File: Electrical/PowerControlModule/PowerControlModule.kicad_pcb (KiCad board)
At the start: 2 copper layers, 2 parts, among them Q1 IPP120P04P4L03AKSA1, Q2 IPP120P04P4L03AKSA1

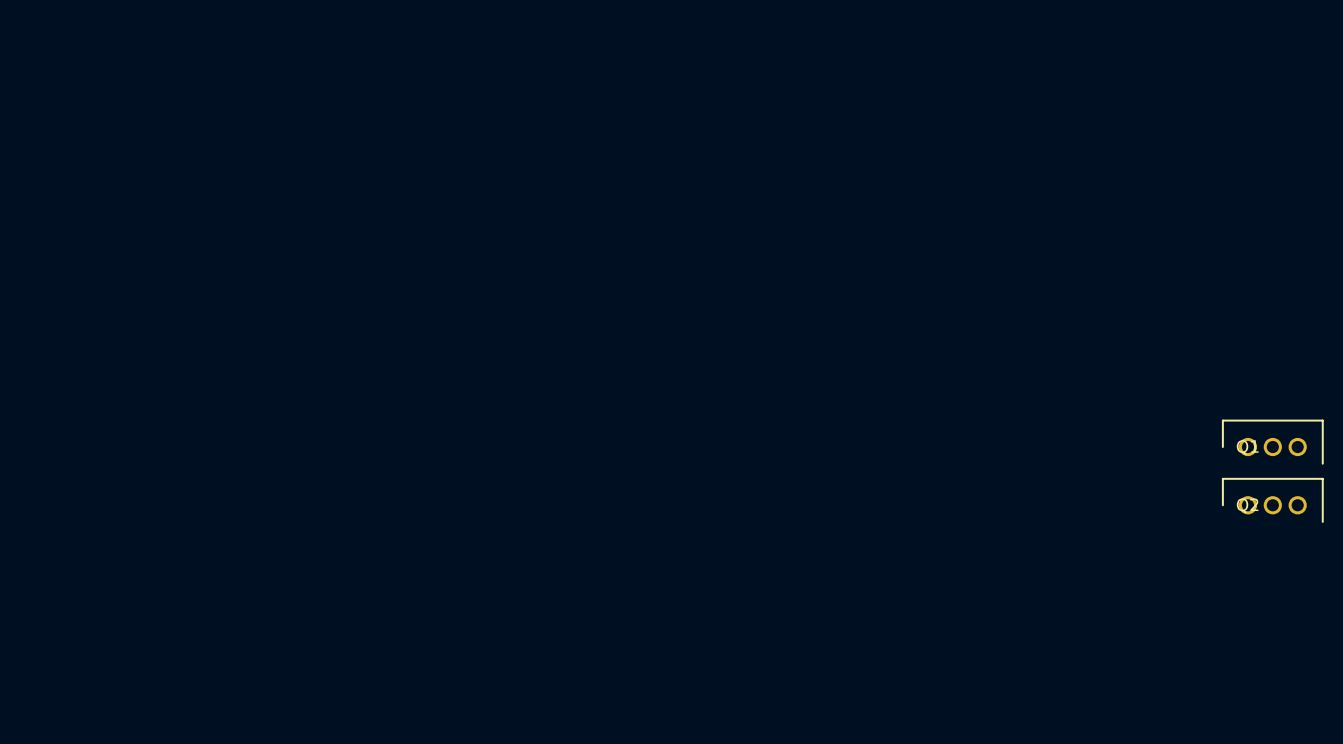
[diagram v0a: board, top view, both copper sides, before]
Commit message: Lays out peripherals and motor control power distribution
Paginates the schematic for ease of editing
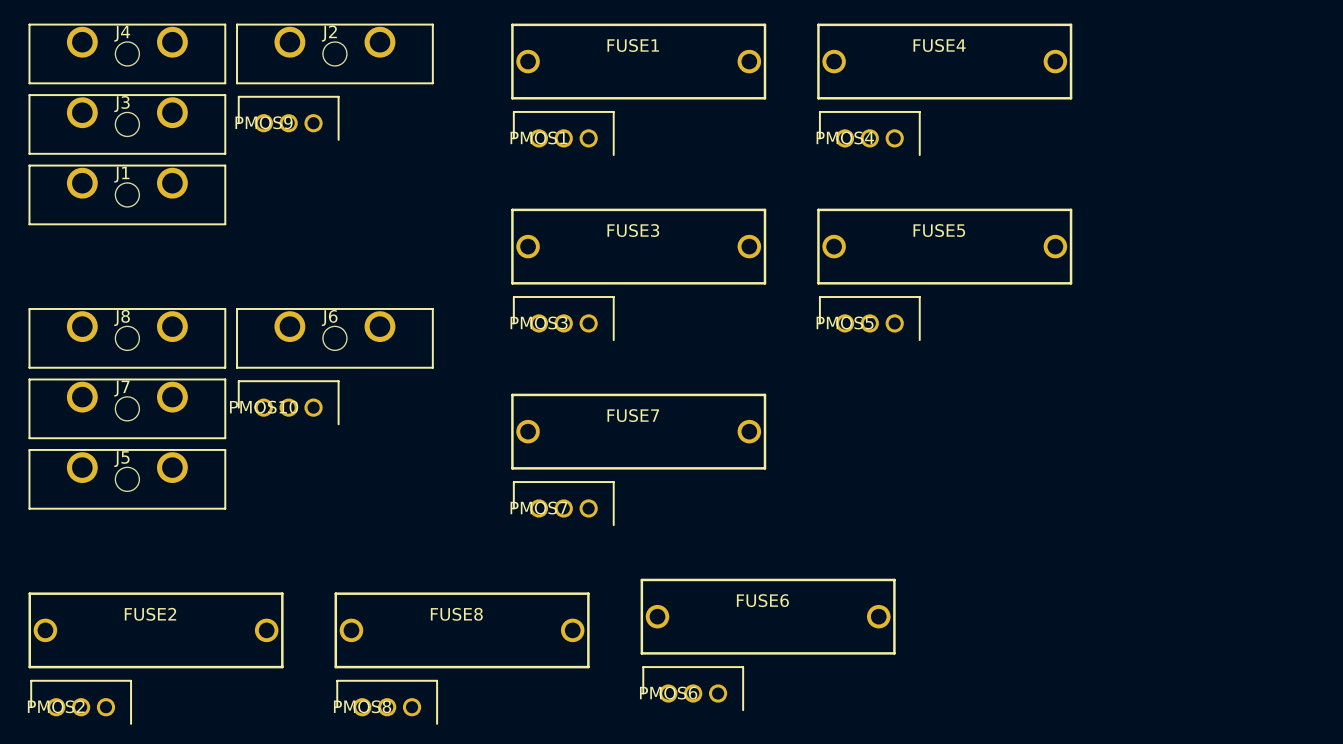
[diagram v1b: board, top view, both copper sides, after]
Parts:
- removed Q1, Q2: IPP120P04P4L03AKSA1, LibraryLoader:TO254P440X1000X2110-3P
- added FUSE1: 64600001003, LibraryLoader:646-SERIESHOLDER, F.Cu at (82.5, 36.8)
- added FUSE2: 64600001003, LibraryLoader:646-SERIESHOLDER, F.Cu at (33.2, 94.9)
- added FUSE3: 64600001003, LibraryLoader:646-SERIESHOLDER, F.Cu at (82.5, 55.7)
- added FUSE4: 64600001003, LibraryLoader:646-SERIESHOLDER, F.Cu at (113.8, 36.8)
- added FUSE5: 64600001003, LibraryLoader:646-SERIESHOLDER, F.Cu at (113.8, 55.7)
- added FUSE6: 64600001003, LibraryLoader:646-SERIESHOLDER, F.Cu at (95.8, 93.5)
- added FUSE7: 64600001003, LibraryLoader:646-SERIESHOLDER, F.Cu at (82.5, 74.6)
- added FUSE8: 64600001003, LibraryLoader:646-SERIESHOLDER, F.Cu at (64.5, 94.9)
- added J1: 178.6164.0002, LibraryLoader:178.6164.0002_1, F.Cu at (30.3, 50.5)
- added J2: 178.6164.0002, LibraryLoader:178.6164.0002_1, F.Cu at (51.5, 36.1)
- added J3: 178.6164.0002, LibraryLoader:178.6164.0002_1, F.Cu at (30.3, 43.3)
- added J4: 178.6164.0002, LibraryLoader:178.6164.0002_1, F.Cu at (30.3, 36.1)
- added J5: 178.6164.0002, LibraryLoader:178.6164.0002_1, F.Cu at (30.3, 79.5)
- added J6: 178.6164.0002, LibraryLoader:178.6164.0002_1, F.Cu at (51.5, 65.1)
- added J7: 178.6164.0002, LibraryLoader:178.6164.0002_1, F.Cu at (30.3, 72.3)
- added J8: 178.6164.0002, LibraryLoader:178.6164.0002_1, F.Cu at (30.3, 65.1)
- added PMOS1: IPP120P04P4L03AKSA1, LibraryLoader:TO254P440X1000X2110-3P, F.Cu at (72.4, 44.7)
- added PMOS10: IPP120P04P4L03AKSA1, LibraryLoader:TO254P440X1000X2110-3P, F.Cu at (44.3, 72.2)
- added PMOS2: IPP120P04P4L03AKSA1, LibraryLoader:TO254P440X1000X2110-3P, F.Cu at (23.1, 102.8)
- added PMOS3: IPP120P04P4L03AKSA1, LibraryLoader:TO254P440X1000X2110-3P, F.Cu at (72.4, 63.6)
- added PMOS4: IPP120P04P4L03AKSA1, LibraryLoader:TO254P440X1000X2110-3P, F.Cu at (103.6, 44.7)
- added PMOS5: IPP120P04P4L03AKSA1, LibraryLoader:TO254P440X1000X2110-3P, F.Cu at (103.6, 63.6)
- added PMOS6: IPP120P04P4L03AKSA1, LibraryLoader:TO254P440X1000X2110-3P, F.Cu at (85.6, 101.4)
- added PMOS7: IPP120P04P4L03AKSA1, LibraryLoader:TO254P440X1000X2110-3P, F.Cu at (72.4, 82.5)
- added PMOS8: IPP120P04P4L03AKSA1, LibraryLoader:TO254P440X1000X2110-3P, F.Cu at (54.3, 102.8)
- added PMOS9: IPP120P04P4L03AKSA1, LibraryLoader:TO254P440X1000X2110-3P, F.Cu at (44.3, 43.1)

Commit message: Adds new part library for SCR stuff. Gets buck converters and connectors to show up on PCB layout
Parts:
- added BUCK1: LM2596, SCR_KiCAD_Lib:LM2596, F.Cu at (167.6, 43.2)
- added BUCK2: LM2596, SCR_KiCAD_Lib:LM2596, F.Cu at (167.6, 91.4)
- added BUCK3: LM2596, SCR_KiCAD_Lib:LM2596, F.Cu at (251.1, 43.2)
- added BUCK4: LM2596, SCR_KiCAD_Lib:LM2596, F.Cu at (167.6, 139.7)
- added BUCK5: LM2596, SCR_KiCAD_Lib:LM2596, F.Cu at (251.1, 139.7)
- added BUCK6: LM2596, SCR_KiCAD_Lib:LM2596, F.Cu at (334.5, 91.4)
- added BUCK7: LM2596, SCR_KiCAD_Lib:LM2596, F.Cu at (334.5, 43.2)
- added BUCK8: LM2596, SCR_KiCAD_Lib:LM2596, F.Cu at (251.1, 91.4)
- added CONN1: Conn_01x02, Connector_PinHeader_2.54mm:PinHeader_1x02_P2.54mm_Vertical, F.Cu at (178.2, 44.8)
- added CONN10: Conn_01x02, Connector_PinHeader_2.54mm:PinHeader_1x02_P2.54mm_Vertical, F.Cu at (329.2, 141.2)
- added CONN11: Conn_01x02, Connector_PinHeader_2.54mm:PinHeader_1x02_P2.54mm_Vertical, F.Cu at (340.8, 141.2)
- added CONN12: Conn_01x02, Connector_PinHeader_2.54mm:PinHeader_1x02_P2.54mm_Vertical, F.Cu at (345.5, 141.2)
- added CONN2: Conn_01x02, Connector_PinHeader_2.54mm:PinHeader_1x02_P2.54mm_Vertical, F.Cu at (178.2, 93.0)
- added CONN3: Conn_01x02, Connector_PinHeader_2.54mm:PinHeader_1x02_P2.54mm_Vertical, F.Cu at (261.7, 44.8)
- added CONN4: Conn_01x02, Connector_PinHeader_2.54mm:PinHeader_1x02_P2.54mm_Vertical, F.Cu at (178.2, 141.2)
- added CONN5: Conn_01x02, Connector_PinHeader_2.54mm:PinHeader_1x02_P2.54mm_Vertical, F.Cu at (261.7, 141.2)
- added CONN6: Conn_01x02, Connector_PinHeader_2.54mm:PinHeader_1x02_P2.54mm_Vertical, F.Cu at (345.1, 93.0)
- added CONN7: Conn_01x02, Connector_PinHeader_2.54mm:PinHeader_1x02_P2.54mm_Vertical, F.Cu at (345.1, 44.8)
- added CONN8: Conn_01x02, Connector_PinHeader_2.54mm:PinHeader_1x02_P2.54mm_Vertical, F.Cu at (261.7, 93.0)
- added CONN9: Conn_01x02, Connector_PinHeader_2.54mm:PinHeader_1x02_P2.54mm_Vertical, F.Cu at (324.6, 141.2)

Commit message: Lays out power distribution board on PCB. Need to make 4 layer setup before routing. Also need to change motor output footprint
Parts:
- removed CONN1, CONN2, CONN3, CONN4, CONN5, CONN6, CONN7, CONN8: Conn_01x02, Connector_PinHeader_2.54mm:PinHeader_1x02_P2.54mm_Vertical
- added J10: Screw_Terminal_01x02, TerminalBlock_Phoenix:TerminalBlock_Phoenix_MKDS-3-2-5.08_1x02_P5.08mm_Horizontal, F.Cu at (145.0, 150.0)
- added J11: Screw_Terminal_01x02, TerminalBlock_Phoenix:TerminalBlock_Phoenix_MKDS-3-2-5.08_1x02_P5.08mm_Horizontal, F.Cu at (145.0, 177.0)
- added J12: Screw_Terminal_01x02, TerminalBlock_Phoenix:TerminalBlock_Phoenix_MKDS-3-2-5.08_1x02_P5.08mm_Horizontal, F.Cu at (145.0, 204.0)
- added J13: Screw_Terminal_01x02, TerminalBlock_Phoenix:TerminalBlock_Phoenix_MKDS-3-2-5.08_1x02_P5.08mm_Horizontal, F.Cu at (145.0, 230.0)
- added J14: Screw_Terminal_01x02, TerminalBlock_Phoenix:TerminalBlock_Phoenix_MKDS-3-2-5.08_1x02_P5.08mm_Horizontal, F.Cu at (145.0, 257.0)
- added J15: Screw_Terminal_01x02, TerminalBlock_Phoenix:TerminalBlock_Phoenix_MKDS-3-2-5.08_1x02_P5.08mm_Horizontal, F.Cu at (145.0, 285.0)
- added J16: Screw_Terminal_01x02, TerminalBlock_Phoenix:TerminalBlock_Phoenix_MKDS-3-2-5.08_1x02_P5.08mm_Horizontal, F.Cu at (145.0, 312.0)
- added J17: Conn_01x03, Connector_Wire:SolderWirePad_1x03_P7.62mm_Drill2.5mm, F.Cu at (19.0, 136.0)
- added J9: Screw_Terminal_01x02, TerminalBlock_Phoenix:TerminalBlock_Phoenix_MKDS-3-2-5.08_1x02_P5.08mm_Horizontal, F.Cu at (145.0, 125.0)
- CONN10, CONN11, CONN12, CONN9: footprint Connector_PinHeader_2.54mm:PinHeader_1x02_P2.54mm_Vertical -> Connector_Wire:SolderWirePad_1x02_P5.08mm_Drill1.5mm
- moved BUCK7 390.3 mm to (33.0, 291.0), turned to 90 degrees
- moved BUCK6 347.4 mm to (33.0, 264.0), turned to 90 degrees
- moved BUCK8 314.5 mm to (33.0, 318.0), turned to 90 degrees
- moved BUCK3 259.6 mm to (33.0, 184.0), turned to 90 degrees
- moved BUCK5 238.8 mm to (33.0, 237.0), turned to 90 degrees
- moved CONN9 230.7 mm to (143.0, -1.00), turned to 270 degrees
- moved FUSE8 222.8 mm to (119.0, 311.0)
- moved CONN10 214.8 mm to (142.0, 36.0), turned to 90 degrees
- moved FUSE7 213.5 mm to (119.0, 285.0)
- moved CONN11 211.1 mm to (144.0, 65.0), turned to 270 degrees
- moved PMOS8 210.8 mm to (87.0, 311.0)
- moved CONN12 205.2 mm to (144.0, 102.0), turned to 90 degrees
- moved PMOS7 202.1 mm to (87.0, 284.0)
- moved FUSE5 174.3 mm to (119.0, 230.0)
- moved FUSE4 167.3 mm to (119.0, 204.0)
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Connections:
- PMOS1 pad 1: /ExtraPeripheral1/ENB -> /ENABLE
- PMOS10 pad 1: /RightMotors/ENB -> /ENABLE
- PMOS2 pad 1: /ExtraPeripheral2/ENB -> /ENABLE
- PMOS3 pad 1: /Camera1/ENB -> /ENABLE
- PMOS4 pad 1: /Camera2/ENB -> /ENABLE
- PMOS5 pad 1: /ODROID/ENB -> /ENABLE
- PMOS6 pad 1: /Sensors/ENB -> /ENABLE
- PMOS7 pad 1: /Nucleo2/ENB -> /ENABLE
- PMOS8 pad 1: /Nucleo1/ENB -> /ENABLE
- PMOS9 pad 1: /LeftMotors/ENB -> /ENABLE
